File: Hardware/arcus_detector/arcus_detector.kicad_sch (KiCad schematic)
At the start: 59 parts, among them J1 Arc_Input, J2 SEN_SEL, J3 ADC_SEL, J4 CAN_connector, U1 TSV911xxLx, U2 ADA2891-4

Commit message: Added parts
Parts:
- removed R19, R? (x3): R, symbol Device:R
- removed U1, U?: TSV911xxLx, Package_TO_SOT_SMD:SOT-23-5, symbol Amplifier_Operational:TSV911xxLx
- removed U2: ADA2891-4, Package_SO:TSSOP-14_4.4x5mm_P0.65mm, symbol my_witch_symbols:ADA4891-4
- added C16: 100u, symbol Device:C
- added C17, C18, C19: 22u, symbol Device:C
- added C20, C21, C24: 10u, symbol Device:C
- added C22: 100p, symbol Device:C
- added C23: 470p, symbol Device:C
- added C25, C26: 0.1u, symbol Device:C
- added C27, C28, C29: 1u, symbol Device:C
- added C30, C31, C32, C33, C34, C35: C OR /, symbol Device:C
- added D1: D_Zener, symbol Device:D_Zener
- added J5, J7: Arc_Input, symbol Connector:Screw_Terminal_01x02
- added J6: FILT_IN_SEL, symbol Connector_Generic:Conn_02x06_Counter_Clockwise
- added R23, R24, R34: R, symbol Device:R
- added R25, R26: 500, symbol Device:R
- added R27: 120, symbol Device:R
- added R28: 10, symbol Device:R
- added R29, R30: 2k2, symbol Device:R
- added R31, R32: 3k3, symbol Device:R
- added R33, R36: R/C, symbol Device:R
- added T1: Transformer_1P_1S, symbol Device:Transformer_1P_1S
- added U1: LD1117S33TR_SOT223, Package_TO_SOT_SMD:SOT-223-3_TabPin2, symbol Regulator_Linear:LD1117S33TR_SOT223
- added U2, U7, U8: MCP6L02x-xSN, Package_SO:SOIC-8_3.9x4.9mm_P1.27mm, symbol Amplifier_Operational:MCP6L02x-xSN
- added U3: SN75176AD, Package_SO:SOIC-8_3.9x4.9mm_P1.27mm, symbol Interface_UART:SN75176AD
- added U4: LD1117S25TR_SOT223, Package_TO_SOT_SMD:SOT-223-3_TabPin2, symbol Regulator_Linear:LD1117S25TR_SOT223
- added U5: MCP662, Package_SO:SOIC-8_3.9x4.9mm_P1.27mm, symbol Amplifier_Operational:MCP6L02x-xSN
- added U6: MCP662-E/MF, Package_SO:SOIC-8_3.9x4.9mm_P1.27mm, symbol Amplifier_Operational:MCP6L02x-xSN
- added U9: MAX11102AUB/V+, symbol my_witch_symbols:MAX11102AUB/V+
- added U?: PRM3W-E12-S5-S1, symbol my_symbols:PRM3W-E12-S5-S
- C1, C15, C2, C3: value C -> 10p
- C14: value 1nF -> 1u
- R10, R11, R14, R15, R18, R20, R21, R22, R6, R9: value R -> R/C
- R17: value R -> R OR /
- Rf: value R -> 30k
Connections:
- net +3V3: now also C1.1, C2.1, C3.1, U?.4 (REF), U?.5 (VDD), U?.8 (OVDD), C20.1, C21.1, C24.1, C25.1, C26.1, U9.4 (REF), U9.5 (VDD), U9.8 (OVDD)
- net +5V: now also C18.1, C19.1, C27.1, C28.1, C29.1, U2.8 (V+), U3.8 (VCC), U5.8 (V+), U6.8 (V+), U7.8 (V+), U8.8 (V+); no longer C15.1
- net ADC_01: now also R25.1
- net GND: now also R10.1, R?.3, C18.2, C19.2, C20.2, C21.2, C23.2, C24.2, C25.2, C26.2, C27.2, C28.2, C29.2, C30.2, C31.2, C32.2, C33.2, C34.2, C35.2, R31.1, R32.1, R36.1, U2.4 (V-), U3.5 (GND), U5.4 (V-), U6.3 (+), U6.4 (V-), U7.4 (V-), U8.4 (V-), U9.11 (EPGND), U9.3 (AGND); no longer C15.2, R13.1, R7.1, R9.1
- net PGA_OUT: now also J6.1 (Pin_1), J6.2 (Pin_2), J6.3 (Pin_3), J6.4 (Pin_4), J6.5 (Pin_5), J6.6 (Pin_6); no longer R10.2, R12.2, R21.1
- net SENS_01: now also U5.1, U5.2 (-)
- net at R21.2, R22.2: now also U2.3 (+)
- net at R17.1: now also U2.1, U2.2 (-)
- net at R20.2: now also R15.2, U7.5 (+)
- net at J3.1 (Pin_1), J3.2 (Pin_2), J3.3 (Pin_3)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: now also U6.1
- net at R3.2, R4.2, R5.2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: now also R23.2, R24.2, U6.2 (-)
- net at R16.1: now also U7.6 (-), U7.7; no longer R15.1
- net FIL4: now reaches R16.2
- net FIL4: now also R8.1, C33.1; no longer R15.2
- net at R11.2: now also R14.2, U7.3 (+); no longer R6.2
- net FIL_IN_2: now reaches R6.1
- net FIL_IN_2: now also J6.11 (Pin_11); no longer R11.1
- net FIL2: now reaches R4.1
- net FIL2: now also R7.2, C31.1
- net at R?.2: now also D1.1 (K)
- net FIL1: now reaches R3.1
- net FIL1: now also R17.2, C30.1
- net at R18.2: now also R9.2, U8.5 (+); no longer R17.2
- net at U?.21 (SCK^{+}): now also R29.1, R31.2
- net at U?.9 (~{CNV}): now also R30.1, R32.2
- net FIL3: now reaches R5.1
- net FIL3: now also R12.2, C32.1
- net ARC_IN renamed ARC_IN_HALL
- net ARC_IN_HALL: now also J5.2 (Pin_2); no longer J1.2 (Pin_2), R?.1
- net ARC_OUT renamed ARC_OUT_HALL
- net ARC_OUT_HALL: now also J5.1 (Pin_1); no longer J1.1 (Pin_1), R?.4
- new net: C23.1, R28.2, U9.1 (AIN1)
- new net: D1.2 (A), U5.3 (+)
- new net: C16.2, U?.1 (GND)
- new net: C16.1, U?.2 (V_{IN})
- new net: C17.1, U?.6 (+Vo)
- new net: C17.2, U?.7 (0V)
- new net: R34.1, U8.1, U8.2 (-)
- new net: R33.2, R36.2, U8.3 (+)
- new net: R12.1, U7.1, U7.2 (-)
- new net: R10.2, R6.2, U2.5 (+)
- new net: R27.1, U3.6 (A)
- new net: R27.2, U3.7 (B)
- new net: R13.1, U8.6 (-), U8.7
- new net: C22.1, R25.2, R26.1, U6.6 (-)
- new net: C22.2, R26.2, R28.1, U6.7
- new net: U3.2 (~{RE}), U3.3 (DE)
- new net: R7.1, U2.6 (-), U2.7
- new net ARC_IN_CT: J7.2 (Pin_2), T1.1 (AA)
- new net ARC_IN_RES: J1.2 (Pin_2), R?.1
- new net ARC_OUT_CT: J7.1 (Pin_1), T1.2 (AB)
- new net ARC_OUT_RES: J1.1 (Pin_1)
- new net FIL5: C34.1, R23.1, R34.2
- new net FIL6: C35.1, R13.2, R24.1
- new net FIL_IN_1: J6.12 (Pin_12), R21.1
- new net FIL_IN_3: J6.10 (Pin_10), R11.1
- new net FIL_IN_4: J6.9 (Pin_9), R15.1
- new net FIL_IN_5: J6.8 (Pin_8), R33.1
- new net FIL_IN_6: J6.7 (Pin_7), R9.1
- new net UART_RX: U3.1 (R)
- new net UART_TX: U3.4 (D)
- new net VDC: U6.5 (+)
- no-connect marks 5 -> 10
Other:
- note added: "MAX11102AUB/V+ / app circuit from datasheet"
- note added: "OP AMP MATRIX FOR FILTERS"
- note added: "OP AMP POWER"
- note added: "SN75175AD"
- note added: "Sensor switch and PGA"
- note removed: "ADA4891-4ARUZ"
- note removed: "ADC circuit 1"
- note removed: "Hall current sensor gets DC from arc, output voltage"
- note removed: "Shunt resistor, how to connect ?"
- note removed: "change op amp to one I use"
- note removed: "https://www.deviceplus.com/others/how-to-measure-circuit-current-with-a-shunt-resistor/"
- note removed: "low pass"
- moved on the sheet: C1, C10, C11, C12, C13, C2, C3, C4, C5, C6, C7, C8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

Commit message: Pin names, CT,
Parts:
- removed C15: 10p, symbol Device:C
- removed C20, C21, C24: 10u, symbol Device:C
- removed C22: 100p, symbol Device:C
- removed C23: 470p, symbol Device:C
- removed C25, C26: 0.1u, symbol Device:C
- removed R25, R26: 500, symbol Device:R
- removed R28: 10, symbol Device:R
- removed unit 2 of U6
- removed U9: MAX11102AUB/V+, symbol my_witch_symbols:MAX11102AUB/V+
- removed U?: LTC2323-12, symbol my_witch_symbols:LTC2323-12
- added C12, C4, C8, C9: 100n, symbol Device:C
- added C27, C40: 10u, symbol Device:C
- added C37: 1u, symbol Device:C
- added C39: 0.1u, symbol Device:C
- added C6, C7: 22u, symbol Device:C
- added R3: 100, symbol Device:R
- added R32: 120, symbol Device:R
- added R4, R5: 10k, symbol Device:R
- added Rf2: 20k, symbol Device:R
- added Rf3: 40k, symbol Device:R
- added U18: LTC2323-12, symbol my_witch_symbols:LTC2323-12
- C10: value 0.1u -> 100n
- C11: value 10u -> 100n
- C13: value 1u -> 100n
- C30: renamed from C18; value 22u -> 10u
- C31: renamed from C5; value C -> 10u
- C32: renamed from C19; value 22u -> 0.1u
- C33: renamed from C4; value C -> 10u
- C34: renamed from C6; value C -> 10u
- Rf1: renamed from Rf; value 30k -> 10k
- U10, U8: renamed from U2; value MCP6L02x-xSN -> MCP662-E/MF
- U10, U12, U9: renamed from U8; value MCP6L02x-xSN -> MCP662-E/MF
- U10, U9: renamed from U7; value MCP6L02x-xSN -> MCP662-E/MF
- U4: renamed from U5; value MCP662 -> MCP662-E/MF
- gave numbers to parts that had none: 11
- renumbered C16 to C1, C30 to C14, C31 to C15, C33 to C16, C35 to C17, C32 to C18, C34 to C19, C17 to C2, C29 to C21, C14 to C22, C27 to C23, C28 to C24, C3 to C25, C2 to C26, C1 to C28, C7 to C29, C8 to C35, C12 to C36, C9 to C38, J5 to J1, J7 to J2, J1 to J3, J2 to J4, J6 to J5, J3 to J6, J4 to J7, R33 to R10, R15 to R11, R10 to R12, R22 to R13, R18 to R15, R36 to R16, R20 to R17, R7 to R18, R17 to R19, R12 to R20, R13 to R21, R34 to R22, R16 to R23, R23 to R24, R24 to R25, R5 to R26, R8 to R27, R3 to R28, R4 to R29, R1 to R30, R2 to R31, R27 to R33, R32 to R34, R31 to R35, R29 to R36, R30 to R37, R21 to R7, R11 to R8, U6 to U12, U3 to U16, U1 to U5, U4 to U6, U6 to U8
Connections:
- net UART_RX is gone; now on net STLINK_RX: U16.1 (R)
- net UART_TX is gone; now on net STLINK_TX: U16.4 (D)
- net +3V3: now also C10.1, C13.1, U15.1 (V_{CC1}), U5.2 (VO), C27.1, C6.1, C8.1, R4.2, U18.1 (V_{DD}), U18.28 (REFINT), U18.8 (V_{DD})
- net +5V: now also C2.1, U2.6 (+Vo), U5.3 (VI), U6.3 (VI), C4.1
- net ADC_03: now also U1.96 (PB1)
- net ARC_OUT_RES: now also R1.4
- net GND: now also C10.2, C11.2, D1.2 (A), U15.4 (GND1), U5.1 (GND), U6.1 (GND), C12.2, C27.2, C37.2, C6.2, C7.2, C8.2, C9.2, R5.1, U18.10 (GND), U18.23 (OGND), U18.25 (~{CMOS}/LVDS), U18.29 (EPGND), U18.4 (GND), U18.5 (GND)
- net VDD: now also C11.1, U6.2 (VO), C12.1, C7.1, C9.1, U18.14 (OV_{DD})
- net at D1.1 (K), R2.2: now also U4.3 (+)
- net at R35.2, R36.1: now also U18.21 (SCK^{+})
- net FDCAN1_TX: now reaches U15.2 (TXD)
- net FDCAN1_TX: now also U1.77 (PB9)
- net FDCAN1_RX: now reaches U15.3 (RXD)
- net FDCAN1_RX: now also U1.75 (PB8)
- net at J7.3 (Pin_3), U15.6 (CANL): now also R32.1
- net at J7.2 (Pin_2), U15.7 (CANH): now also R32.2
- net SPI1_SCK: now reaches R36.2
- net SPI1_SCK: now also U1.83 (PA5), U17.10 (SCLK)
- net at R24.2, R25.2, R26.2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: now also Rf2.1, Rf3.1
- net at C36.1: now also U18.13 (VBYP1)
- net at C2.2, U2.7 (0V): now also C4.2
- net at C35.1, C38.1: now also U18.12 (REFOUT1)
- net at C35.2, C38.2: now also U18.11 (REFRTN1)
- net at J6.1 (Pin_1), J6.2 (Pin_2), J6.3 (Pin_3)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: now also Rf2.2, Rf3.2
- net SENS_03: now reaches J4.3 (Pin_3)
- net SENS_03: now also T1.4 (SB), R3.2
- net at C29.1, R30.2: now also U18.7 (A_{IN1+})
- net at C29.2, R31.2: now also U18.6 (A_{IN1-})
- net USART3_RTS/DE: now reaches U1.100 (LD3/PB14)
- net USART3_RTS/DE: now also U16.2 (~{RE}), U16.3 (DE)
- net USART3_CTS/NSS: now reaches U1.102 (ETH_TXD1/PB13)
- net SPI1_NSS: now reaches U1.32 (PA4)
- net SPI1_NSS: now also R37.2, U17.6 (~{CS})
- net SPI4_SCK: now reaches U1.46 (PE2)
- net SPI4_SCK: now also U7.7 (SCK)
- net SPI4_NSS: now reaches U1.48 (PE4)
- net SPI4_NSS: now also U7.5 (~{CS})
- net SPI4_MISO: now reaches U1.50 (PE5)
- net SPI4_MOSI: now reaches U1.62 (PE6)
- net SPI4_MOSI: now also U7.6 (SI)
- net USB_OTG_FS_DP: now reaches U1.84 (USB_DP/PA12)
- net SPI1_MISO: now reaches U1.85 (PA6)
- net SPI1_MISO: now also U17.9 (DOUT), U18.15 (SDO1^{+})
- net USB_OTG_FS_DM: now reaches U1.86 (USB_DM/PA11)
- net SPI1_MOSI: now reaches U1.87 (ETH_CRS_DV/PA7)
- net USART3_CK: now reaches U1.88 (PB12)
- net STLINK_RX: now reaches U1.90 (PB11)
- net USB_OTG_FS_VBUS: now reaches U1.93 (USB_VBUS/PA9)
- net USB_OTG_FS_SOF: now reaches U1.95 (USB_SOF/PA8)
- net STLINK_TX: now reaches U1.97 (PB10)
- net CH_SEL: now reaches U1.98 (PB15)
- net CH_SEL: now also U17.7 (CHSEL)
- net at R34.2, R37.1: now also U18.9 (~{CNV})
- net at T1.3 (SA): now also R3.1, R4.1, R5.2
- new net: C39.1, C40.1, U18.26 (REFOUT2)
- new net: C39.2, C40.2, U18.27 (REFRTN2)
- new net: C37.1, U18.24 (VBYP2)
- no-connect marks 10 -> 119
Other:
- note added: "A PINS PA4 - SPI1_NSS PA5 - SPI1_SCK PA6 - SPI1_MISO PA7 - SPI1_MOSI PA8 - USB_OTG_FS_SOF PA9 - USB_OTG_FS_VBUS PA11 - USB_OTG_FS_DM PA12 - USB_OTG_FS_DP"
- note added: "B PINS PB1 - ADC1_IN5 INTERNAL ADC PB8 - CAN1_RX PB9 - CAN1_TX PB10 - USART3_TX / STLINK_TX PB11 - USART3_RX STLINK_RX PB12 - USART3_CK PB13 - USART3_CTS/NSS PB14 - USART3_RTS/DE PB15 - CH_SEL, GPIO OUTPUT"
- note added: "E PINS PE2 - SPI4_SCK PE4 - SPI4_NSS PE5 - SPI4_MISO PE6 - SPI4_MOSI"
- note added: "ISO1042"
- note added: "POWER UNIT"
- note added: "PROVISIONAL PINOUT LIST"
- note removed: "3 ADCS, 2 EXTERNAL, ONE FROM STM"
- note removed: "3 sensor block hall, tc and shunt + opamps"
- note removed: "CAN TRANSCIEVERS , 2 ISO1042DWR"
- note removed: "ISOLATED DC/DC , PART OF POWER UNIT"
- note removed: "MATRIX OF OPAMPS / TO CREATE FILTERS IN THE FUTURE"
- note removed: "MAX11102AUB/V+ / app circuit from datasheet"
- note removed: "MCP6S91-E/MS / PGA"
- note removed: "RS 845"
- note removed: "SUMMING OPAMP / ARRAY OF RESISTORS AND AMP OF 1"
- note removed: "SWITCH BETWEEN FILTERS"
- note removed: "output of sensor is going to a switch , that is not a switch but a pin header so we manually switch"
- moved on the sheet: C1, C2, C29, C3, C30, C31, C32, C33, C34, C35, C36, C38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

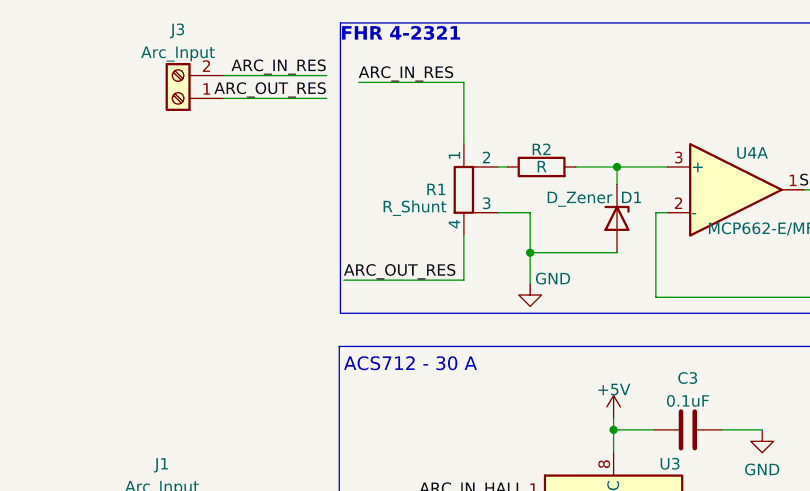
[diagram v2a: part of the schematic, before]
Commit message: -added uart buffer writer -measurement code -restructuded project
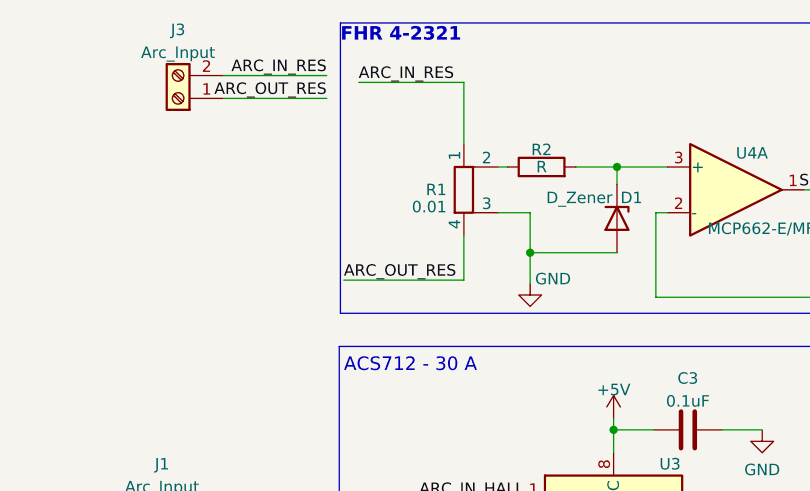
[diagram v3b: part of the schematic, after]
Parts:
- R1: value R_Shunt -> 0.01
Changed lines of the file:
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@@
       (effects (font (size 1.27 1.27)) (justify right))
     )
-    (property "Value" "R_Shunt" (at 46.863 33.909 0)
+    (property "Value" "0.01" (at 46.863 33.909 0)
       (effects (font (size 1.27 1.27)) (justify right))
     )

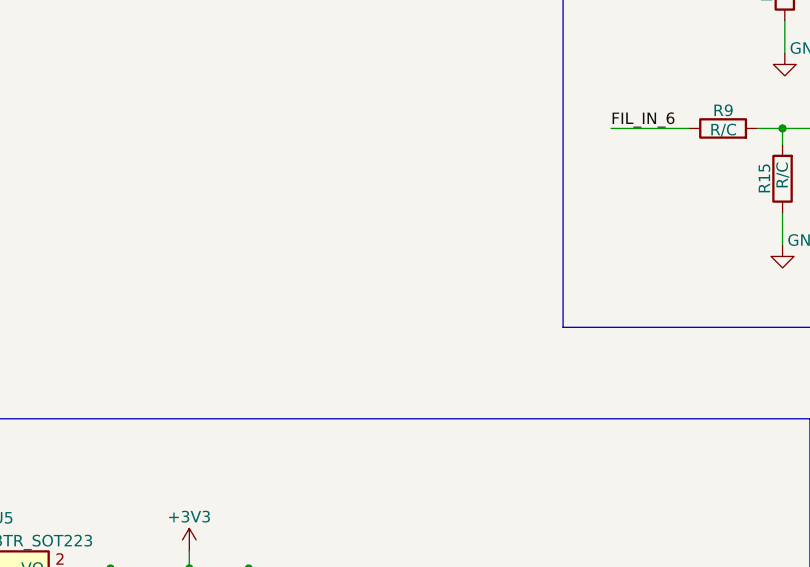
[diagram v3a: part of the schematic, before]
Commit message: -added another sheet in kicad - PGA code added
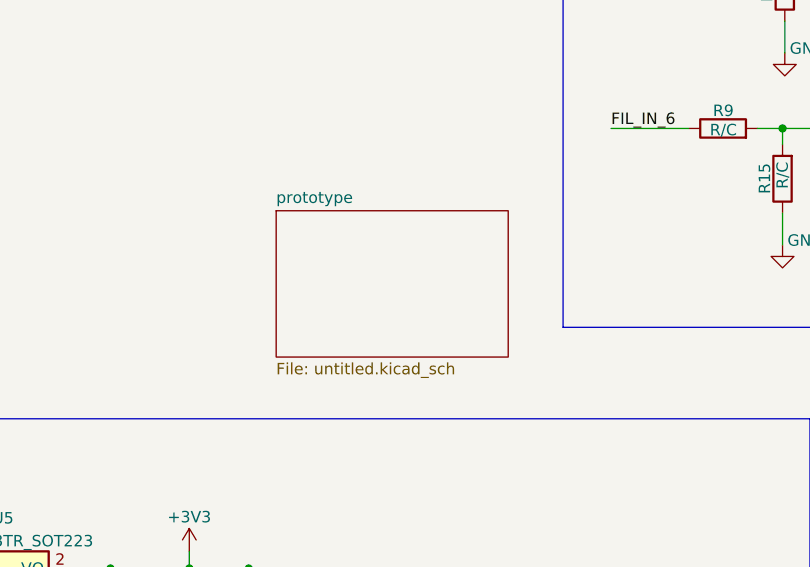
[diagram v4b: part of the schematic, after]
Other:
- added sheet prototype (untitled.kicad_sch)
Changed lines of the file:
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@@
+    )
+  )
+  (sheet (at 119.507 186.944) (size 25.781 16.256) (fields_autoplaced)
+    (stroke (width 0.1524) (type solid))
+    (fill (color 0 0 0 0.0000))
+    (property "Sheetname" "prototype" (at 119.507 186.2324 0)
+      (effects (font (size 1.27 1.27)) (justify left bottom))
+    )
+    (property "Sheetfile" "untitled.kicad_sch" (at 119.507 203.7846 0)
+      (effects (font (size 1.27 1.27)) (justify left top))
+    )
+    (instances
+      (project "arcus_detector"
+        (path "/1075cd99-b527-424a-8676-af3337dfe390" (page "2"))
+      )
     )
   )
